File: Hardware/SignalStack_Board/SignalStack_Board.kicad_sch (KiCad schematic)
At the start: 67 parts, among them J1 Molex_uF_SV_06, J2 RJ45_LED_Shielded, Q1 SI4156DY, Q2 SI4156DY, Q3 SI4156DY, Q4 SI4156DY, Q5 SI4156DY, Q6 SI4156DY, Q7 SI4156DY, Q8 SI4156DY, U1 OKI, U2 Teensy4.1_DEV-16771, U3 IRS2005S, U4 IRS2005S, U5 IRS2005S, U6 IRS2005S, U7 MMC5633NJL, U8 SMAJ12CA

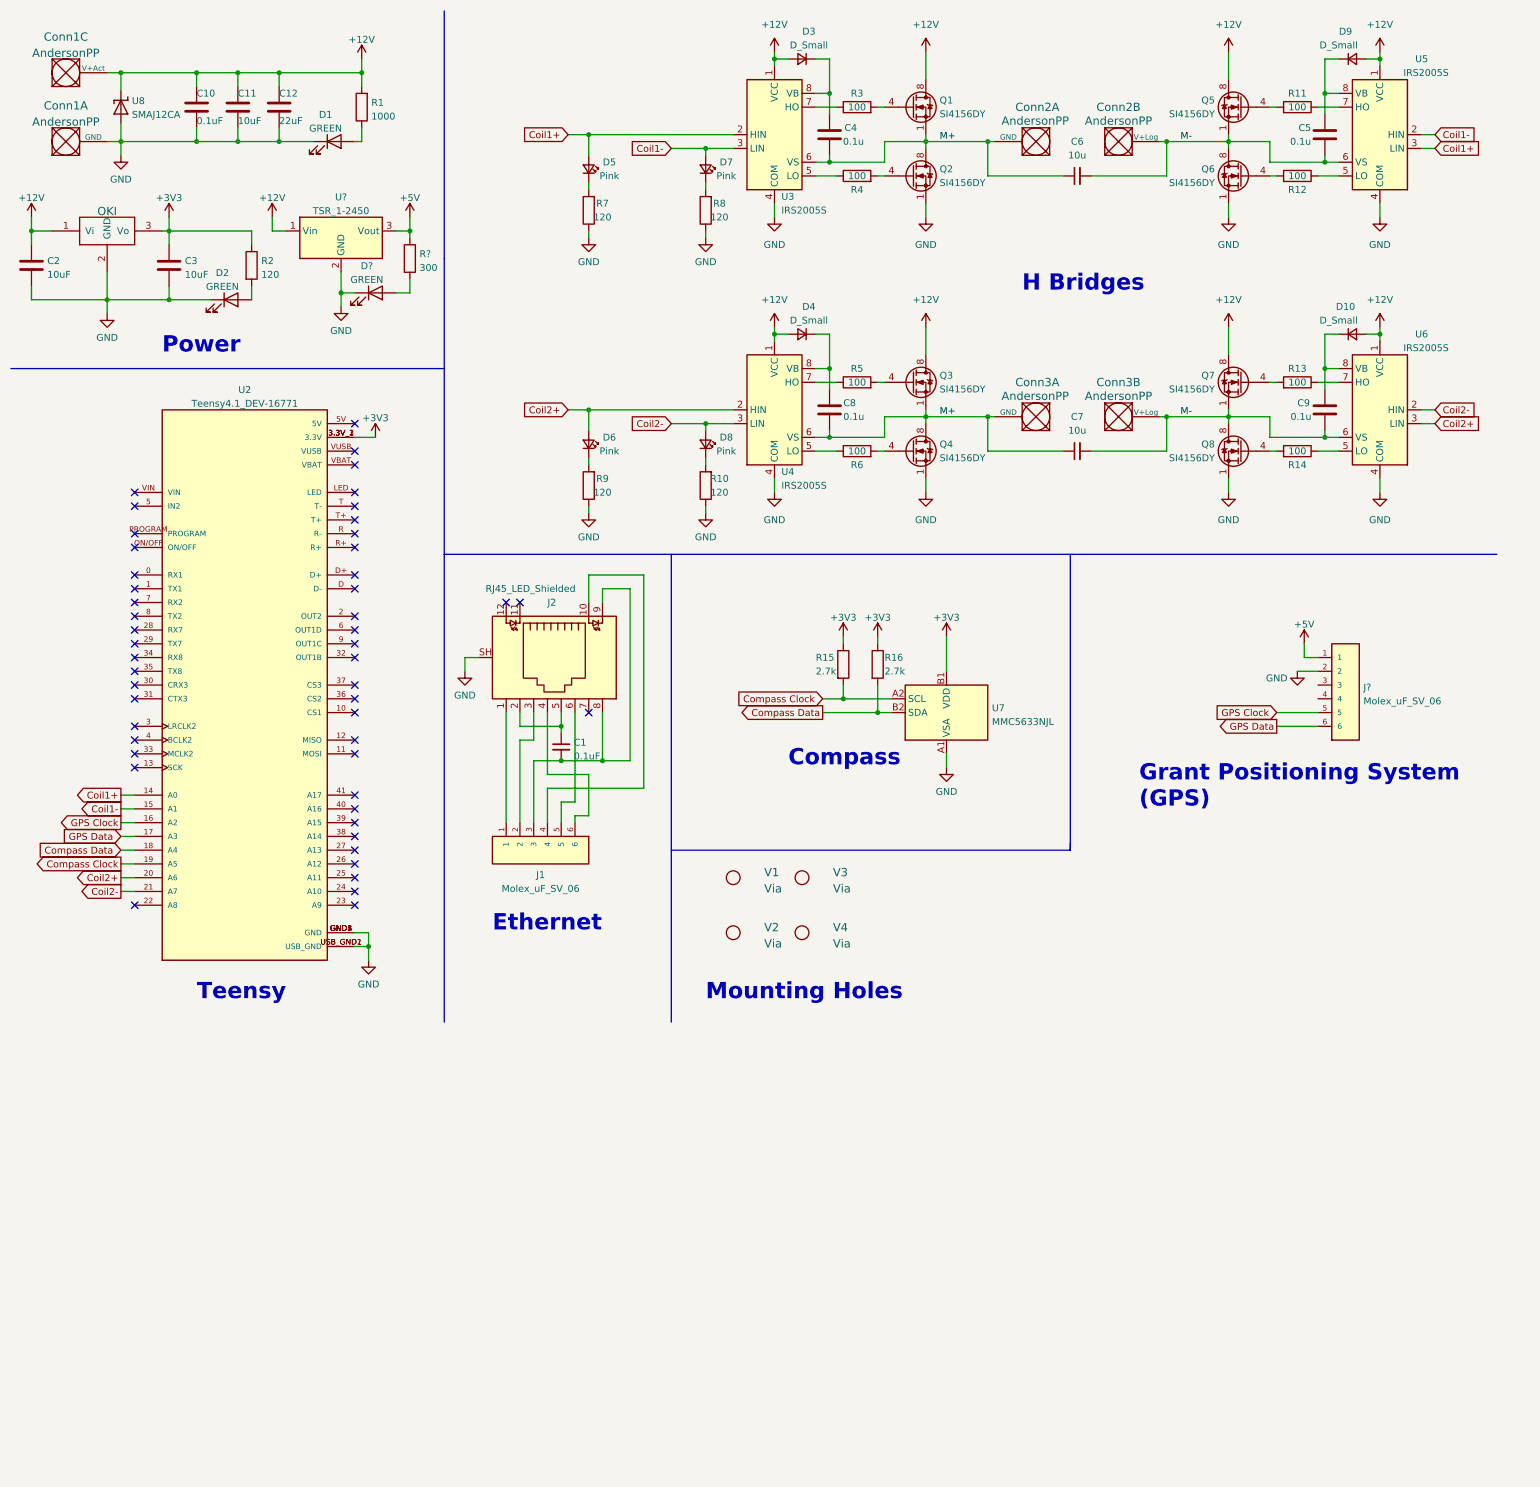
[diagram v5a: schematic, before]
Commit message: Assigned footprints
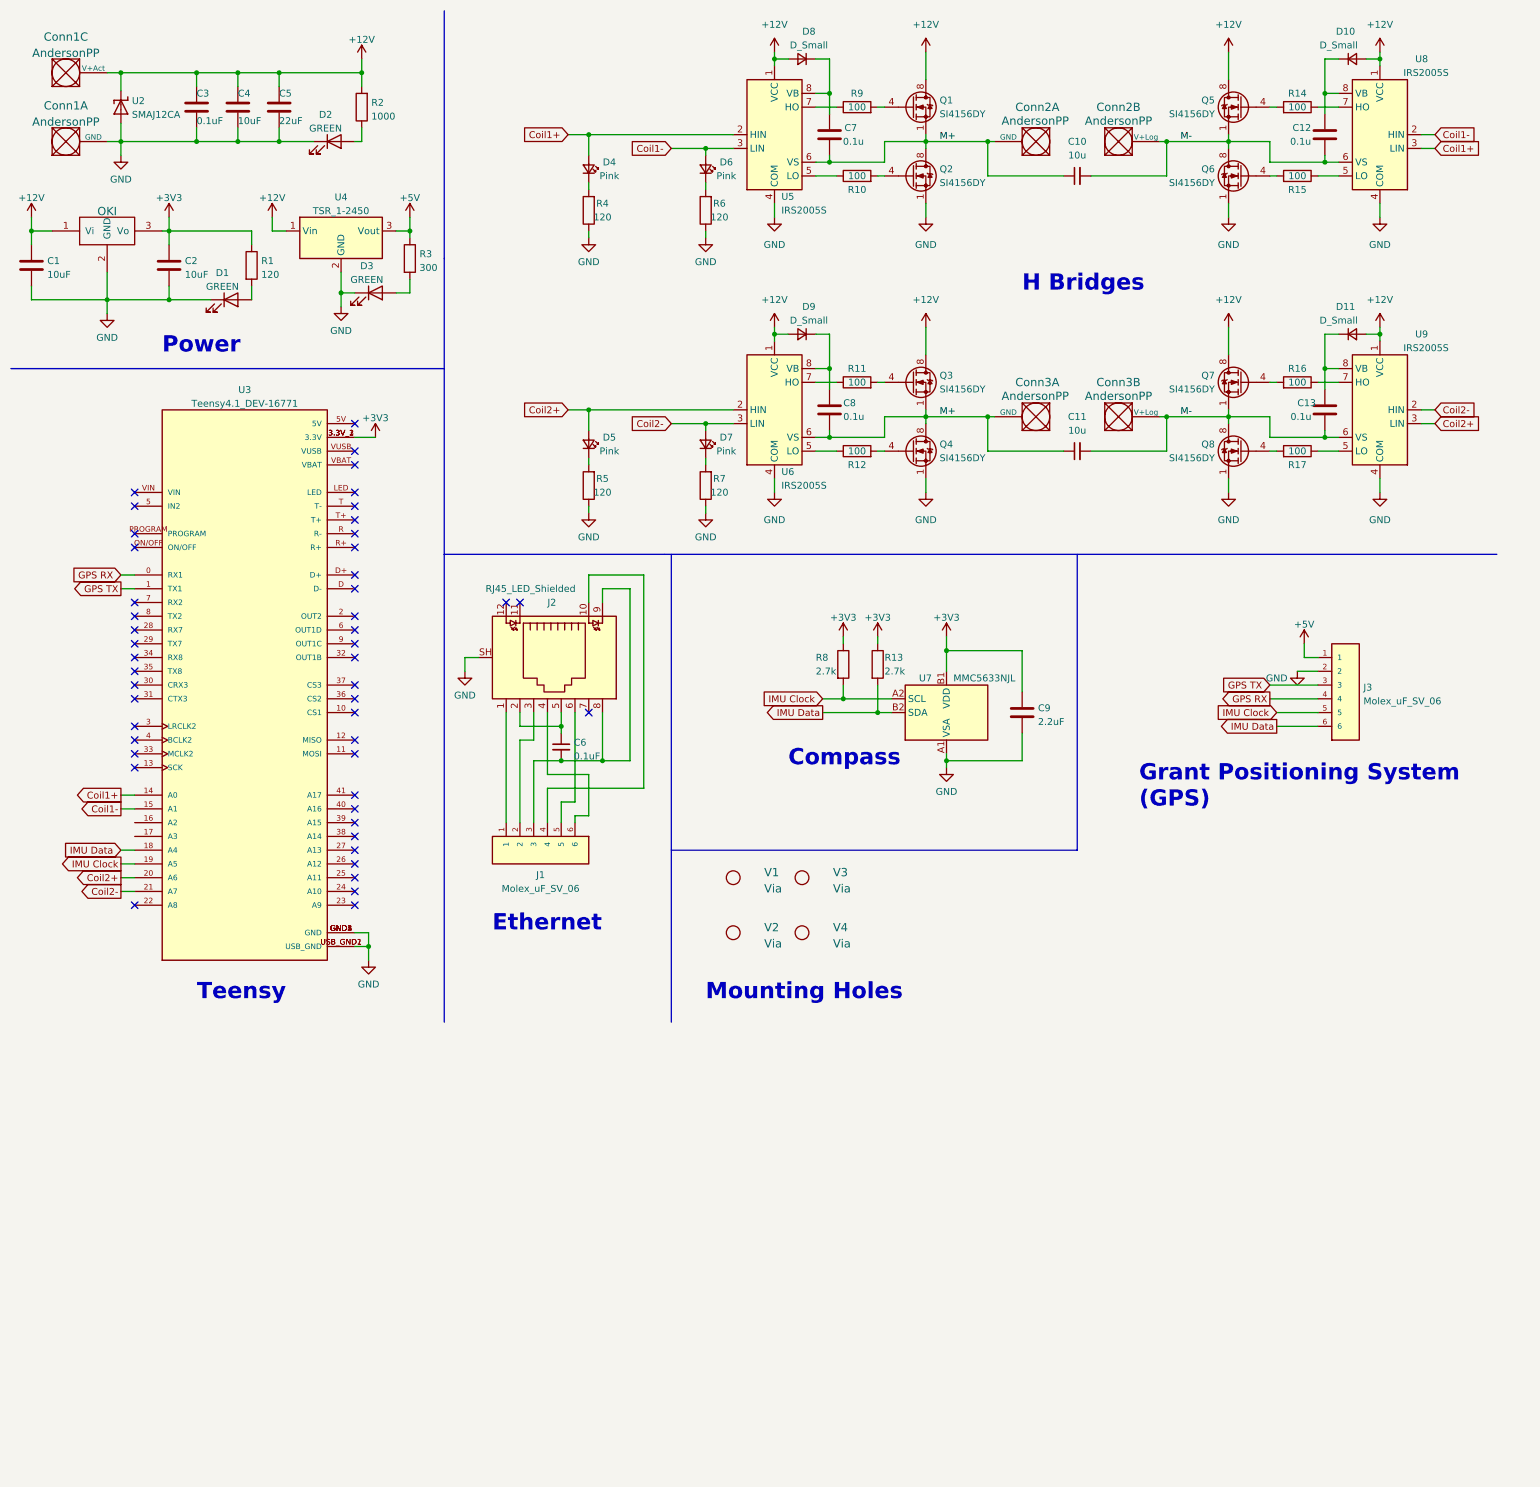
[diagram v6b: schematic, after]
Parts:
- added C9: 2.2uF, Capacitor_SMD:C_0603_1608Metric_Pad1.08x0.95mm_HandSolder, symbol Device:C
- C1: renamed from C2; footprint (none) -> Capacitor_SMD:C_0603_1608Metric_Pad1.08x0.95mm_HandSolder
- C10: renamed from C6; footprint (none) -> Capacitor_SMD:C_0603_1608Metric_Pad1.08x0.95mm_HandSolder
- C11: renamed from C7; footprint (none) -> Capacitor_SMD:C_0603_1608Metric_Pad1.08x0.95mm_HandSolder
- C12: renamed from C5; footprint Capacitor_SMD:C_0603_1608Metric -> Capacitor_SMD:C_0603_1608Metric_Pad1.08x0.95mm_HandSolder
- C13: renamed from C9; footprint Capacitor_SMD:C_0603_1608Metric -> Capacitor_SMD:C_0603_1608Metric_Pad1.08x0.95mm_HandSolder
- C2: renamed from C3; footprint (none) -> Capacitor_SMD:C_0603_1608Metric_Pad1.08x0.95mm_HandSolder
- C3: renamed from C10; footprint (none) -> Capacitor_SMD:C_0603_1608Metric_Pad1.08x0.95mm_HandSolder
- C4: renamed from C11; footprint (none) -> Capacitor_SMD:C_0603_1608Metric_Pad1.08x0.95mm_HandSolder
- C5: renamed from C12; footprint (none) -> Capacitor_SMD:C_0603_1608Metric_Pad1.08x0.95mm_HandSolder
- C6: renamed from C1; footprint (none) -> Capacitor_SMD:C_0603_1608Metric_Pad1.08x0.95mm_HandSolder
- C7: renamed from C4; footprint Capacitor_SMD:C_0603_1608Metric -> Capacitor_SMD:C_0603_1608Metric_Pad1.08x0.95mm_HandSolder
- C8: footprint Capacitor_SMD:C_0603_1608Metric -> Capacitor_SMD:C_0603_1608Metric_Pad1.08x0.95mm_HandSolder
- Conn1: footprint (none) -> MRDT_Connectors:Anderson_2_Horizontal_Side_by_Side
- D1: renamed from D2; footprint (none) -> Diode_SMD:D_0603_1608Metric_Pad1.05x0.95mm_HandSolder
- D10: renamed from D9; footprint (none) -> Diode_SMD:D_0603_1608Metric_Pad1.05x0.95mm_HandSolder
- D11: renamed from D10; footprint (none) -> Diode_SMD:D_0603_1608Metric_Pad1.05x0.95mm_HandSolder
- D2: renamed from D1; footprint (none) -> Diode_SMD:D_0603_1608Metric_Pad1.05x0.95mm_HandSolder
- D3: renamed from D?; footprint (none) -> Diode_SMD:D_0603_1608Metric_Pad1.05x0.95mm_HandSolder
- D4: renamed from D5; footprint (none) -> Diode_SMD:D_0603_1608Metric_Pad1.05x0.95mm_HandSolder
- D5: renamed from D6; footprint (none) -> Diode_SMD:D_0603_1608Metric_Pad1.05x0.95mm_HandSolder
- D6: renamed from D7; footprint (none) -> Diode_SMD:D_0603_1608Metric_Pad1.05x0.95mm_HandSolder
- D7: renamed from D8; footprint (none) -> Diode_SMD:D_0603_1608Metric_Pad1.05x0.95mm_HandSolder
- D8: renamed from D3; footprint (none) -> Diode_SMD:D_0603_1608Metric_Pad1.05x0.95mm_HandSolder
- D9: renamed from D4; footprint (none) -> Diode_SMD:D_0603_1608Metric_Pad1.05x0.95mm_HandSolder
- J2: footprint (none) -> MRDT_Connectors:RJ45_Teensy
- R1: renamed from R2; footprint (none) -> Resistor_SMD:R_0603_1608Metric_Pad0.98x0.95mm_HandSolder
- R13: renamed from R16; footprint (none) -> Resistor_SMD:R_0603_1608Metric_Pad0.98x0.95mm_HandSolder
- R2: renamed from R1; footprint (none) -> Resistor_SMD:R_0603_1608Metric_Pad0.98x0.95mm_HandSolder
- R3: renamed from R?; footprint (none) -> Resistor_SMD:R_0603_1608Metric_Pad0.98x0.95mm_HandSolder
- R8: renamed from R15; footprint (none) -> Resistor_SMD:R_0603_1608Metric_Pad0.98x0.95mm_HandSolder
- U1: footprint (none) -> MRDT_Devices:OKI_Horizontal
- U2: renamed from U8; footprint DO-214AC -> MRDT_Actives:DO-214AC
- U3: renamed from U2; footprint MODULE_DEV-16771 -> MRDT_Shields:Teensy_4_1_Vertical
- V1, V2, V3, V4: footprint (none) -> MRDT_Drill_Holes:4_40_Hole_Corner
- gave numbers to parts that had none: 2
- renumbered R4 to R10, R5 to R11, R6 to R12, R11 to R14, R12 to R15, R13 to R16, R14 to R17, R7 to R4, R9 to R5, R8 to R6, R10 to R7, R3 to R9, U3 to U5, U4 to U6, U5 to U8, U6 to U9
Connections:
- net +3V3: now also C9.1
- net GND: now also C9.2
- net GPS TX: now reaches J3.3
- net GPS TX: now also U3.1 (TX1)
- net GPS RX: now reaches J3.4
- net GPS RX: now also U3.0 (RX1)
- net Compass Clock renamed IMU Clock
- net IMU Clock: now also J3.5
- net Compass Data renamed IMU Data
- net IMU Data: now also J3.6
- net GPS Clock: no longer names the net of U3.16 (A2)
- net GPS Clock: no longer J3.5
- net GPS Data: no longer names the net of U3.17 (A3)
- net GPS Data: no longer J3.6
- no-connect marks 50 -> 48

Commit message: Finished schematic
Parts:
- removed C9: 2.2uF, Capacitor_SMD:C_0603_1608Metric_Pad1.08x0.95mm_HandSolder, symbol Device:C
- removed R13, R8: 2.7k, Resistor_SMD:R_0603_1608Metric_Pad0.98x0.95mm_HandSolder, symbol Device:R
- removed U7: MMC5633NJL, Package_BGA:WLP-4_0.86x0.86mm_P0.4mm, symbol Sensor_Magnetic:MMC5633NJL
- U4: footprint Converter_DCDC:Converter_DCDC_TRACO_TSR-1_THT -> MRDT_Devices:TSR_1-2433
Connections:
- net IMU Data: no longer J3.6
- net IMU Clock renamed I2C SCL
- new net I2C SDA: J3.6
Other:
- note removed: "Compass"
- moved on the sheet: J3

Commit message: Worked on layout a lot
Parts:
- removed unit 3 of Conn1
- added unit 2 of Conn1
- J1: footprint MRDT_Connectors:MOLEX_uF_S_06_Vertical -> Connector_PinHeader_2.00mm:PinHeader_2x03_P2.00mm_Vertical
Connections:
- net +12V: now also Conn1.2 (V+Log)
- net TX+: now reaches J1.1, J2.1
- net TX-: now reaches J1.2, J2.3
- net RX+: now reaches J1.6, J2.4
- net RX-: now reaches J1.5, J2.6
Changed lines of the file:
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@@
     (effects (font (size 3 3) (thickness 0.6) bold) (justify left bottom))
+  )
+  (label "TX+" (at 102.87 160.02 90)
+    (effects (font (size 1.27 1.27)) (justify left bottom))
   )
   (label "M+" (at 182.88 86.36 0)
     (effects (font (size 1.27 1.27)) (justify left bottom))
   )
+  (label "RX-" (at 113.03 160.02 90)
+    (effects (font (size 1.27 1.27)) (justify left bottom))
+  )
   (label "M+" (at 182.88 35.56 0)
     (effects (font (size 1.27 1.27)) (justify left bottom))
   )
+  (label "TX-" (at 105.41 160.02 90)
+    (effects (font (size 1.27 1.27)) (justify left bottom))
+  )
   (label "M-" (at 227.33 86.36 0)
+    (effects (font (size 1.27 1.27)) (justify left bottom))
+  )
+  (label "RX+" (at 118.11 160.02 90)
     (effects (font (size 1.27 1.27)) (justify left bottom))
   )
@@
     (pin "1")
   )
-  (symbol (lib_id "MRDT_Connectors:AndersonPP") (at 19.05 38.1 0) (unit 1)
-    (in_bom yes) (on_board yes) (fields_autoplaced)
-    (property "Reference" "Conn1" (id 0) (at 21.59 28.9359 0)
+  (symbol (lib_id "MRDT_Connectors:AndersonPP") (at 19.05 25.4 0) (unit 2)
+    (in_bom yes) (on_board yes) (fields_autoplaced)
+    (property "Reference" "Conn1" (id 0) (at 21.59 16.2359 0)
       (effects (font (size 1.524 1.524)))
     )
-    (property "Value" "AndersonPP" (id 1) (at 21.59 31.9293 0)
+    (property "Value" "AndersonPP" (id 1) (at 21.59 19.2293 0)
       (effects (font (size 1.524 1.524)))
     )
-    (property "Footprint" "MRDT_Connectors:Anderson_2_Horizontal_Side_by_Side" (id 2) (at 15.24 52.07 0)
-      (effects (font (size 1.524 1.524)) hide)
-    )
-    (property "Datasheet" "" (id 3) (at 15.24 52.07 0)
+    (property "Footprint" "MRDT_Connectors:Anderson_2_Horizontal_Side_by_Side" (id 2) (at 15.24 39.37 0)
+      (effects (font (size 1.524 1.524)) hide)
+    )
+    (property "Datasheet" "" (id 3) (at 15.24 39.37 0)
       (effects (font (size 1.524 1.524)) hide)
     )
@@
     (pin "2")
   )
+  (symbol (lib_id "MRDT_Connectors:AndersonPP") (at 19.05 38.1 0) (unit 1)
+    (in_bom yes) (on_board yes) (fields_autoplaced)
+    (property "Reference" "Conn1" (id 0) (at 21.59 28.9359 0)
+      (effects (font (size 1.524 1.524)))
+    )
+    (property "Value" "AndersonPP" (id 1) (at 21.59 31.9293 0)
+      (effects (font (size 1.524 1.524)))
+    )
+    (property "Footprint" "MRDT_Connectors:Anderson_2_Horizontal_Side_by_Side" (id 2) (at 15.24 52.07 0)
+      (effects (font (size 1.524 1.524)) hide)
+    )
+    (property "Datasheet" "" (id 3) (at 15.24 52.07 0)
+      (effects (font (size 1.524 1.524)) hide)
+    )
+    (pin "1")
+    (pin "2")
+    (pin "3")
+    (pin "4")
+    (pin "1")
+  )
   (symbol (lib_id "power:+12V") (at 59.69 49.53 0) (unit 1)
     (in_bom yes) (on_board yes) (fields_autoplaced)
@@
     (pin "2")
   )
-  (symbol (lib_id "MRDT_Connectors:AndersonPP") (at 19.05 25.4 0) (unit 3)
-    (in_bom yes) (on_board yes) (fields_autoplaced)
-    (property "Reference" "Conn1" (id 0) (at 21.59 16.2359 0)
-      (effects (font (size 1.524 1.524)))
-    )
-    (property "Value" "AndersonPP" (id 1) (at 21.59 19.2293 0)
-      (effects (font (size 1.524 1.524)))
-    )
-    (property "Footprint" "MRDT_Connectors:Anderson_2_Horizontal_Side_by_Side" (id 2) (at 15.24 39.37 0)
-      (effects (font (size 1.524 1.524)) hide)
-    )
-    (property "Datasheet" "" (id 3) (at 15.24 39.37 0)
-      (effects (font (size 1.524 1.524)) hide)
-    )
-    (pin "1")
-    (pin "2")
-    (pin "3")
-    (pin "4")
-    (pin "1")
-  )
   (symbol (lib_id "Device:C_Small") (at 113.03 147.32 0) (unit 1)
     (in_bom yes) (on_board yes) (fields_autoplaced)
@@
     (property "Reference" "J1" (id 0) (at 109.22 170.9404 90))
     (property "Value" "Molex_uF_SV_06" (id 1) (at 109.22 173.4773 90))
-    (property "Footprint" "MRDT_Connectors:MOLEX_uF_S_06_Vertical" (id 2) (at 107.95 166.37 0)
+    (property "Footprint" "Connector_PinHeader_2.00mm:PinHeader_2x03_P2.00mm_Vertical" (id 2) (at 107.95 166.37 0)
       (effects (font (size 1.27 1.27)) (justify left bottom) hide)
     )
@@
       (reference "C13") (unit 1) (value "0.1u") (footprint "Capacitor_SMD:C_0603_1608Metric_Pad1.08x0.95mm_HandSolder")
     )
-    (path "/413d518a-123b-4404-a6e1-7163a7cf98bd"
+    (path "/c059550b-e967-4b7c-8d54-2cc4b7e0eff1"
       (reference "Conn1") (unit 1) (value "AndersonPP") (footprint "MRDT_Connectors:Anderson_2_Horizontal_Side_by_Side")
     )
-    (path "/dbd410fd-276f-4a12-a3be-5d5a2853b564"
-      (reference "Conn1") (unit 3) (value "AndersonPP") (footprint "MRDT_Connectors:Anderson_2_Horizontal_Side_by_Side")
+    (path "/4470fd7a-32a9-4a7f-937a-98c8610c7077"
+      (reference "Conn1") (unit 2) (value "AndersonPP") (footprint "MRDT_Connectors:Anderson_2_Horizontal_Side_by_Side")
     )
     (path "/f402e432-547b-44fa-9c6b-b785a1b7d57e"
@@
     )
     (path "/f28ab78a-6455-4e49-bb99-4e4c94db59e5"
-      (reference "J1") (unit 1) (value "Molex_uF_SV_06") (footprint "MRDT_Connectors:MOLEX_uF_S_06_Vertical")
+      (reference "J1") (unit 1) (value "Molex_uF_SV_06") (footprint "Connector_PinHeader_2.00mm:PinHeader_2x03_P2.00mm_Vertical")
     )
     (path "/92825f4f-110c-4978-9182-e1e2e0698ce4"
